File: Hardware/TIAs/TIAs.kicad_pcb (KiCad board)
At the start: 2 copper layers, 33.5 x 33.5 mm, 16 parts, among them U1 Opamp_Dual

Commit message: Added Labels
should be ready for a board review?
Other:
- board text added: "PD Breakout, MRDT, MS&T, 2023"
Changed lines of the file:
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@@
   (gr_arc (start 78.105 96.012) (mid 75.231319 94.821682) (end 74.041 91.948)
     (stroke (width 0.15) (type default)) (layer "Edge.Cuts"))
+  (gr_text "PD Breakout, MRDT,\nMS&T, 2023" (at 97.9932 93.472) (layer "B.SilkS")
+    (effects (font (size 1 1) (thickness 0.15)) (justify left bottom mirror))
+  )
   (segment (start 89.5731 66.6242) (end 85.2316 70.9657) (width 0.254) (layer "F.Cu") (net 1))
   (segment (start 85.2316 70.9657) (end 84.582 70.9657) (width 0.254) (layer "F.Cu") (net 1))

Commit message: Fixed footprints
Some resistors still had LED footprints which I had thought I had fixed, but failed because I did not also update the schematic.
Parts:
- R1, R2, R3, R5: footprint LED_SMD:LED_0603_1608Metric_Pad1.05x0.95mm_HandSolder -> Resistor_SMD:R_0603_1608Metric_Pad0.98x0.95mm_HandSolder
- moved R3 0.46 mm to (96.9, 93.4)

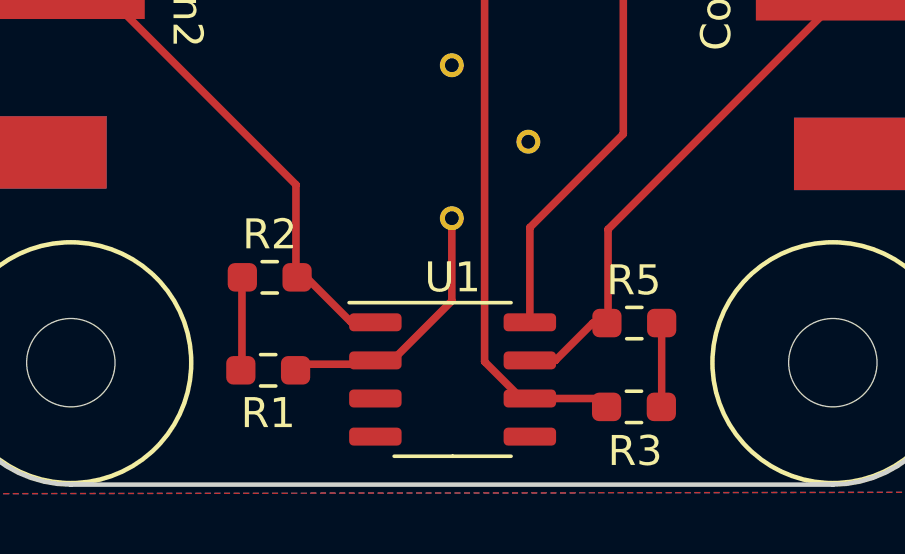
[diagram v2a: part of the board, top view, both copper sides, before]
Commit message: Fixed 68 errors
It works now hopefully?
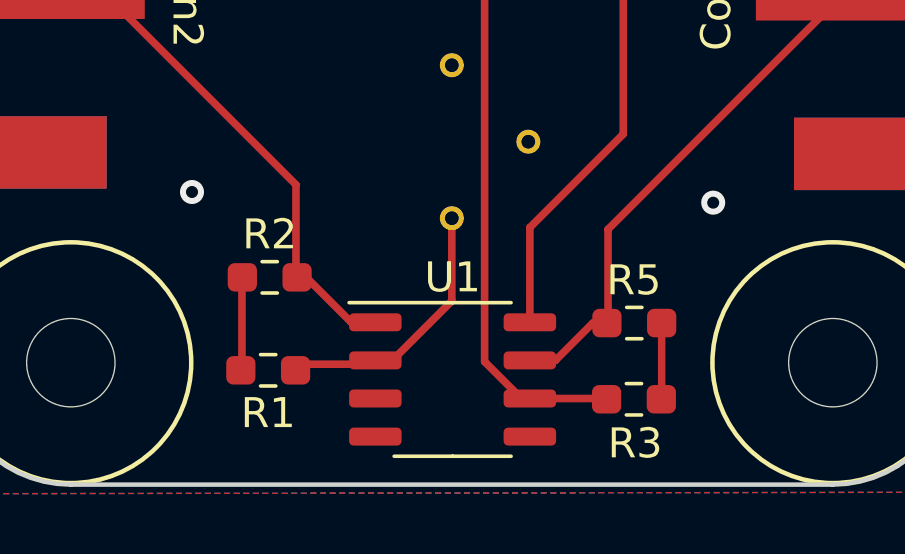
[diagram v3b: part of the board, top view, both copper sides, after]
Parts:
- moved R3 0.25 mm to (96.9, 93.2)
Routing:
- net GND: vias 0 -> 2
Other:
- board text added: "Photodiode Breakout, Rev1 Mars Rover Design Team Missouri S&T, 2023"
- board text removed: "PD Breakout, MRDT, MS&T, 2023"
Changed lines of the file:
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@@
   )
   (footprint "Resistor_SMD:R_0603_1608Metric_Pad0.98x0.95mm_HandSolder" (layer "F.Cu")
-    (at 96.8756 93.4212)
+    (at 96.8756 93.1672)
     (descr "Resistor SMD 0603 (1608 Metric), square (rectangular) end terminal, IPC_7351 nominal with elongated pad for handsoldering. (Body size source: IPC-SM-782 page 72, https://www.pcb-3d.com/wordpress/wp-content/uploads/ipc-sm-782a_amendment_1_and_2.pdf), generated with kicad-footprint-generator")
     (tags "resistor handsolder")
@@
   (gr_arc (start 78.105 96.012) (mid 75.231319 94.821682) (end 74.041 91.948)
     (stroke (width 0.15) (type default)) (layer "Edge.Cuts"))
-  (gr_text "PD Breakout, MRDT,\nMS&T, 2023" (at 97.282 93.4212) (layer "B.SilkS")
-    (effects (font (size 1 1) (thickness 0.15)) (justify left bottom mirror))
+  (gr_text "Photodiode Breakout, Rev1 \nMars Rover Design Team\nMissouri S&T, 2023" (at 99.1108 94.742) (layer "B.SilkS")
+    (effects (font (size 1.016 0.8128) (thickness 0.15)) (justify left bottom mirror))
   )
   (segment (start 89.5731 66.6242) (end 85.2316 70.9657) (width 0.254) (layer "F.Cu") (net 1))
@@
   (segment (start 96.52 73.5711) (end 89.5731 66.6242) (width 0.254) (layer "F.Cu") (net 1))
   (segment (start 93.4054 87.4426) (end 96.52 84.328) (width 0.254) (layer "F.Cu") (net 1))
+  (via (at 99.5172 86.614) (size 0.8) (drill 0.4) (layers "F.Cu" "B.Cu") (net 2))
+  (via (at 82.1436 86.2584) (size 0.8) (drill 0.4) (layers "F.Cu" "B.Cu") (net 2))
   (segment (start 84.582 69.1407) (end 84.582 66.8642) (width 0.254) (layer "F.Cu") (net 3))
   (segment (start 90.805 89.8906) (end 90.805 87.132) (width 0.254) (layer "F.Cu") (net 4))
@@
   (segment (start 91.8972 76.2762) (end 91.8972 91.91318) (width 0.254) (layer "F.Cu") (net 7))
   (segment (start 93.12582 93.1418) (end 93.4054 93.1418) (width 0.254) (layer "F.Cu") (net 7))
-  (segment (start 95.6837 93.1418) (end 95.9631 93.4212) (width 0.254) (layer "F.Cu") (net 7))
+  (segment (start 95.9377 93.1418) (end 95.9631 93.1672) (width 0.254) (layer "F.Cu") (net 7))
   (segment (start 91.8972 91.91318) (end 93.12582 93.1418) (width 0.254) (layer "F.Cu") (net 7))
   (segment (start 89.535 73.914) (end 91.8972 76.2762) (width 0.254) (layer "F.Cu") (net 7))
-  (segment (start 93.4054 93.1418) (end 95.6837 93.1418) (width 0.254) (layer "F.Cu") (net 7))
-  (segment (start 97.7995 90.6272) (end 97.7995 93.4098) (width 0.25) (layer "F.Cu") (net 8))
-  (segment (start 97.7995 93.4098) (end 97.7881 93.4212) (width 0.25) (layer "F.Cu") (net 8))
+  (segment (start 93.4054 93.1418) (end 95.9377 93.1418) (width 0.254) (layer "F.Cu") (net 7))
+  (segment (start 97.7995 90.6272) (end 97.7995 93.1558) (width 0.25) (layer "F.Cu") (net 8))
+  (segment (start 97.7995 93.1558) (end 97.7881 93.1672) (width 0.25) (layer "F.Cu") (net 8))
   (segment (start 96.012 87.503) (end 96.012 90.5897) (width 0.254) (layer "F.Cu") (net 9))
   (segment (start 95.9745 90.6272) (end 95.504 90.6272) (width 0.254) (layer "F.Cu") (net 9))

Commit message: Minor Finishing Touches
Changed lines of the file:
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@@
     (pad "2" smd rect (at -5.588 0 180) (size 5.08 2.413) (layers "F.Cu" "F.Paste" "F.Mask")
       (net 2 "GND") (pinfunction "Sleve") (pintype "input"))
-    (pad "2" smd rect (at -5.588 0 180) (size 5.08 2.413) (layers "B.Cu" "F.Paste" "F.Mask")
+    (pad "2" smd rect (at -5.588 0 180) (size 5.08 2.413) (layers "B.Cu" "B.Paste" "B.Mask")
       (net 2 "GND") (pinfunction "Sleve") (pintype "input"))
     (pad "2" smd rect (at 5.588 0 180) (size 5.08 2.413) (layers "F.Cu" "F.Paste" "F.Mask")
       (net 2 "GND") (pinfunction "Sleve") (pintype "input"))
-    (pad "2" smd rect (at 5.588 0 180) (size 5.08 2.413) (layers "B.Cu" "F.Paste" "F.Mask")
+    (pad "2" smd rect (at 5.588 0 180) (size 5.08 2.413) (layers "B.Cu" "B.Paste" "B.Mask")
       (net 2 "GND") (pinfunction "Sleve") (pintype "input"))
   )
@@
     (pad "2" smd rect (at -5.588 0) (size 5.08 2.413) (layers "F.Cu" "F.Paste" "F.Mask")
       (net 2 "GND") (pinfunction "Sleve") (pintype "input"))
-    (pad "2" smd rect (at -5.588 0) (size 5.08 2.413) (layers "B.Cu" "F.Paste" "F.Mask")
+    (pad "2" smd rect (at -5.588 0) (size 5.08 2.413) (layers "B.Cu" "B.Paste" "B.Mask")
       (net 2 "GND") (pinfunction "Sleve") (pintype "input"))
     (pad "2" smd rect (at 5.588 0) (size 5.08 2.413) (layers "F.Cu" "F.Paste" "F.Mask")
       (net 2 "GND") (pinfunction "Sleve") (pintype "input"))
-    (pad "2" smd rect (at 5.588 0) (size 5.08 2.413) (layers "B.Cu" "F.Paste" "F.Mask")
+    (pad "2" smd rect (at 5.588 0) (size 5.08 2.413) (layers "B.Cu" "B.Paste" "B.Mask")
       (net 2 "GND") (pinfunction "Sleve") (pintype "input"))
   )
@@
   (gr_arc (start 78.105 96.012) (mid 75.231319 94.821682) (end 74.041 91.948)
     (stroke (width 0.15) (type default)) (layer "Edge.Cuts"))
-  (gr_text "Photodiode Breakout, Rev1 \nMars Rover Design Team\nMissouri S&T, 2023" (at 99.1108 94.742) (layer "B.SilkS")
-    (effects (font (size 1.016 0.8128) (thickness 0.15)) (justify left bottom mirror))
+  (gr_text "Photodiode Breakout, Rev1 \nMars Rover Design Team\nMissouri S&T, 2023" (at 83.185 80.01) (layer "F.SilkS")
+    (effects (font (size 1.016 0.8128) (thickness 0.15)) (justify left bottom))
   )
   (segment (start 89.5731 66.6242) (end 85.2316 70.9657) (width 0.254) (layer "F.Cu") (net 1))

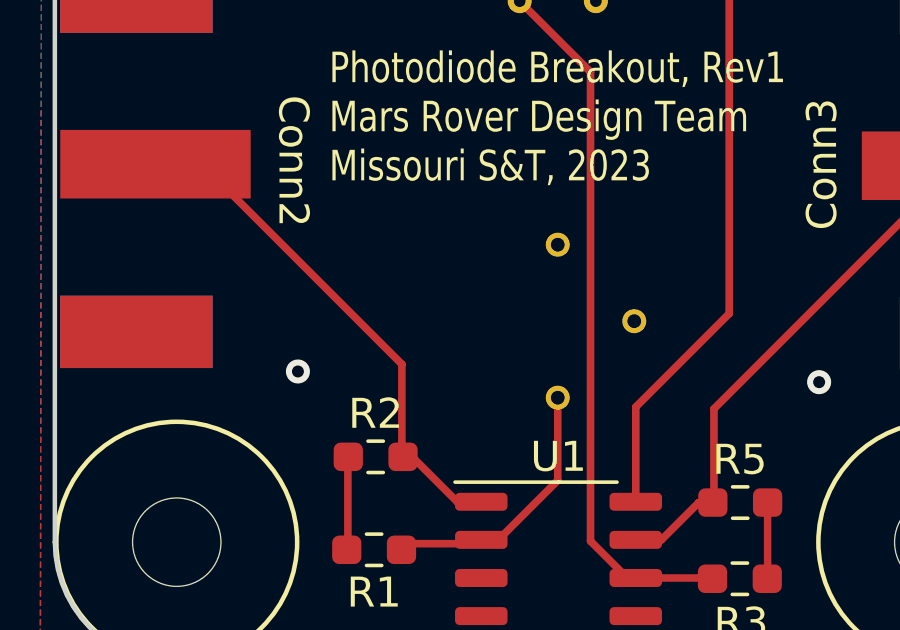
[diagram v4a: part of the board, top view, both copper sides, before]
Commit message: Added names to mini boards
Drew told me to
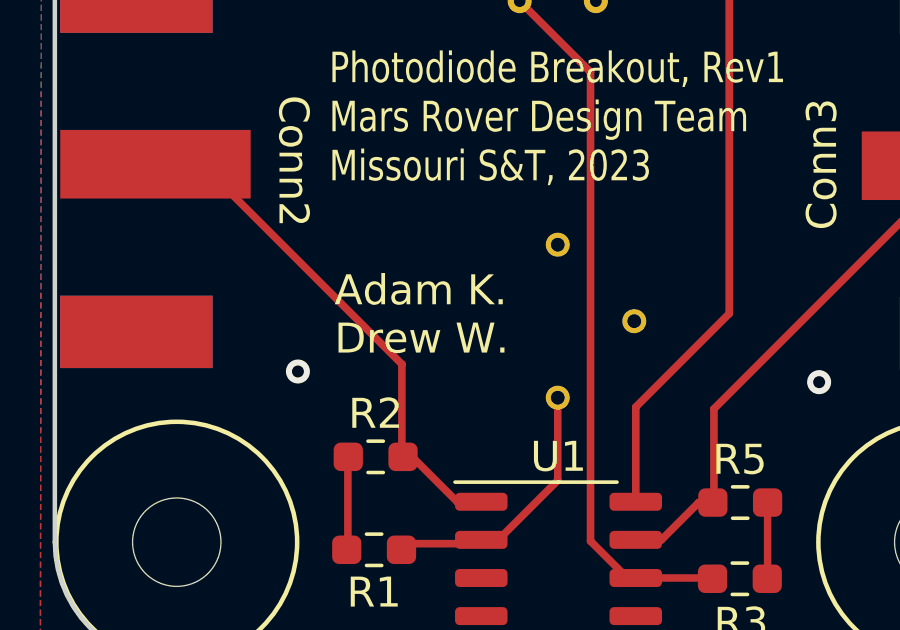
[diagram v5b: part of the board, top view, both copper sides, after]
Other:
- board text added: "Adam K. Drew W."
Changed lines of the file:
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@@
     (effects (font (size 1.016 0.8128) (thickness 0.15)) (justify left bottom))
+  )
+  (gr_text "Adam K.\nDrew W." (at 83.3628 85.7504) (layer "F.SilkS")
+    (effects (font (size 1 1) (thickness 0.15)) (justify left bottom))
   )
   (segment (start 89.5731 66.6242) (end 85.2316 70.9657) (width 0.254) (layer "F.Cu") (net 1))
